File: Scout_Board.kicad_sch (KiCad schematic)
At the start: 6 parts, among them U1 DRV8871DDA, U2 ESP32-S3-DEVKITC-1U-N8R2

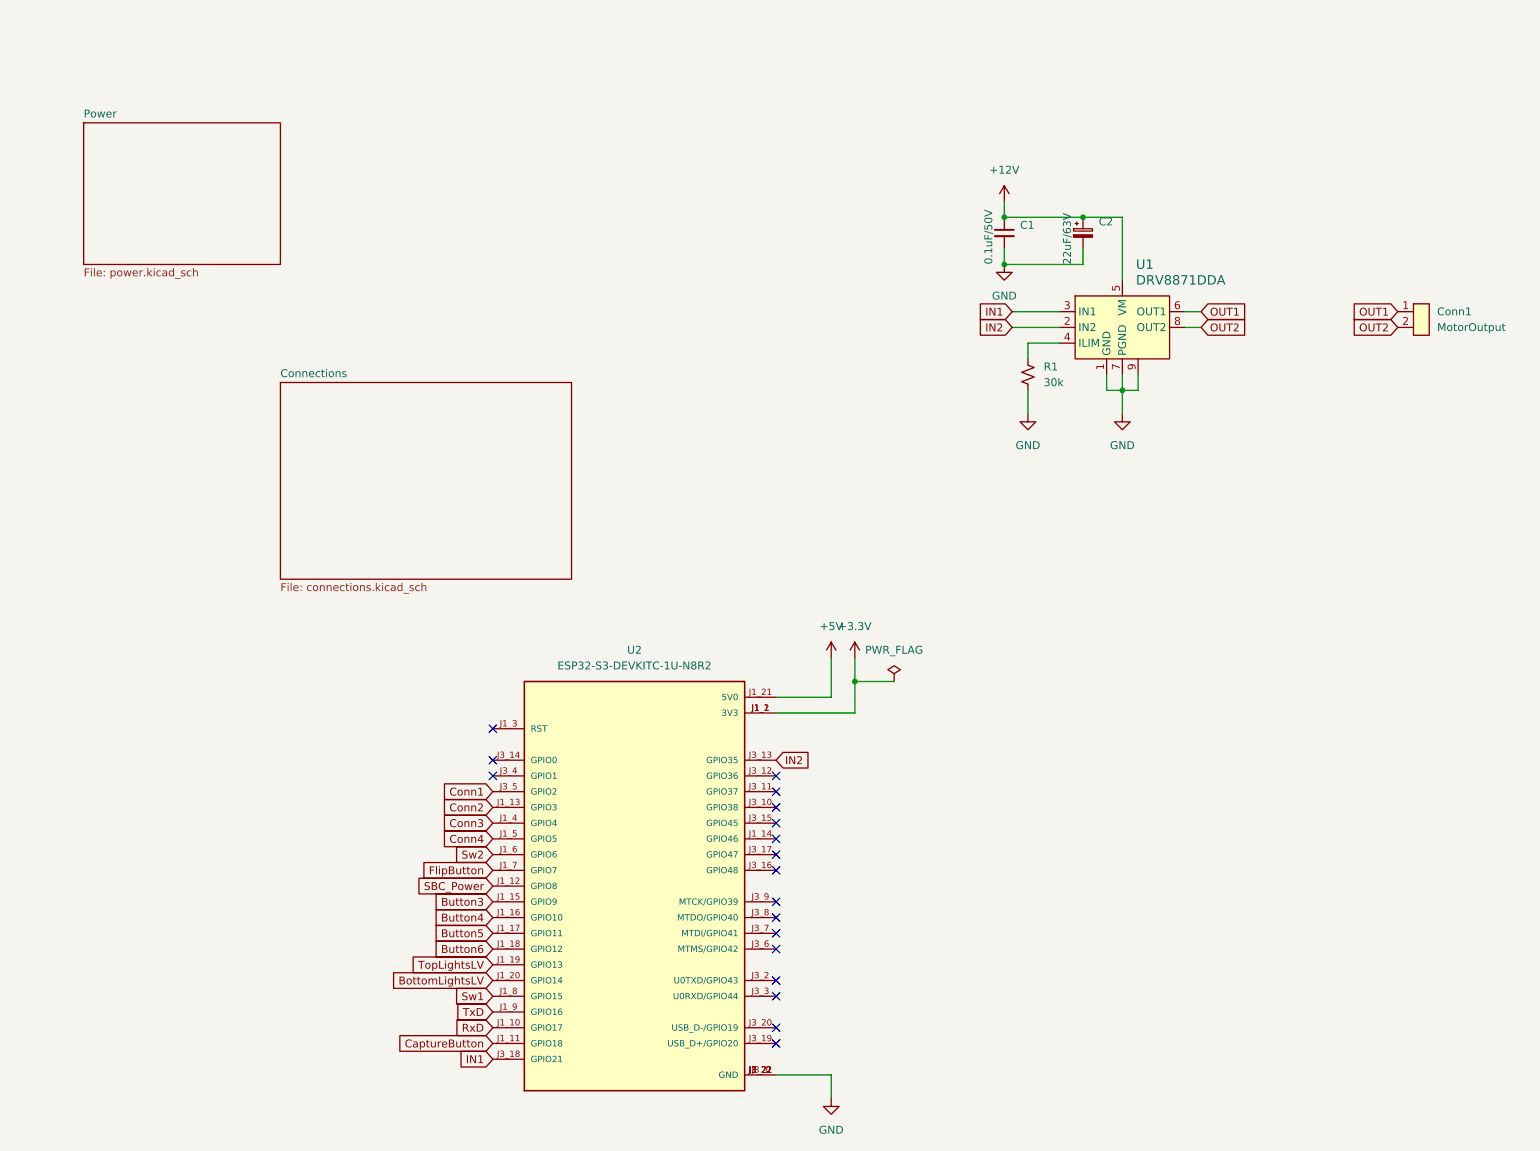
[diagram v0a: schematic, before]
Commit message: Removed motor and added A4988
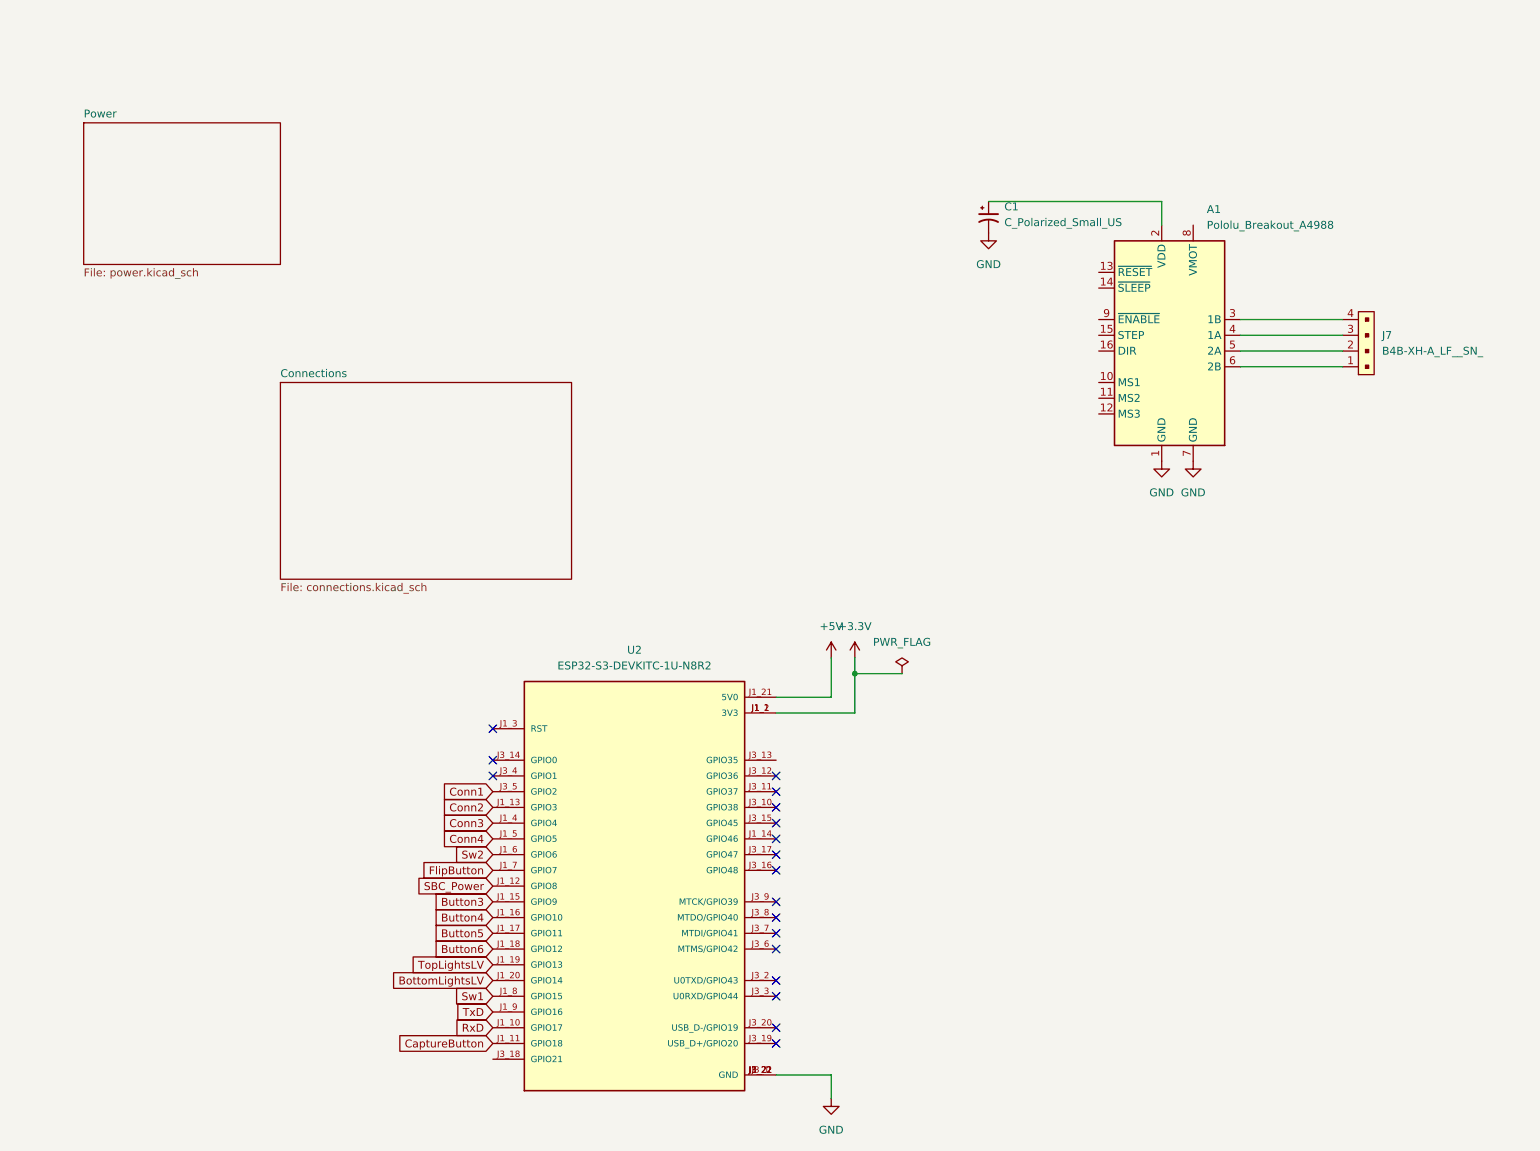
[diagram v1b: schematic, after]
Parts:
- removed C1: 0.1uF/50V, Capacitor_SMD:C_0603_1608Metric_Pad1.08x0.95mm_HandSolder, symbol Device:C_Small
- removed C2: 22uF/63V, EEH_ZA1J220XP:CAP_EEHZA1J220XP, symbol Device:C_Polarized_Small
- removed Conn1: MotorOutput, Downloaded_footprints:CONN_B2B-ZRLFSN_JST, symbol Scout_library:B2B_VERT_1.5MM
- removed R1: 30k, Resistor_SMD:R_0603_1608Metric_Pad0.98x0.95mm_HandSolder, symbol Device:R_Small_US
- removed U1: DRV8871DDA, Package_SO:Texas_HTSOP-8-1EP_3.9x4.9mm_P1.27mm_EP2.95x4.9mm_Mask2.4x3.1mm_ThermalVias, symbol dk_PMIC-Motor-Drivers-Controllers:DRV8871DDA
- added A1: Pololu_Breakout_A4988, Module:Pololu_Breakout-16_15.2x20.3mm, symbol Driver_Motor:Pololu_Breakout_A4988
- added C1: C_Polarized_Small_US, symbol Device:C_Polarized_Small_US
- added J7: B4B-XH-A_LF__SN_, digikey-footprints:PinHeader_1x4_P2mm_Drill1mm, symbol dk_Rectangular-Connectors-Headers-Male-Pins:B4B-XH-A_LF__SN_
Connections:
- net GND: now also A1.1 (GND), A1.7 (GND), C1.2
- net IN1: no longer names the net of U2.J3_18 (GPIO21)
- net IN2: no longer names the net of U2.J3_13 (GPIO35)
- new net: A1.2 (VDD), C1.1
- new net: A1.6 (2B), J7.1
- new net: A1.5 (2A), J7.2
- new net: A1.4 (1A), J7.3
- new net: A1.3 (1B), J7.4

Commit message: Added motor driver
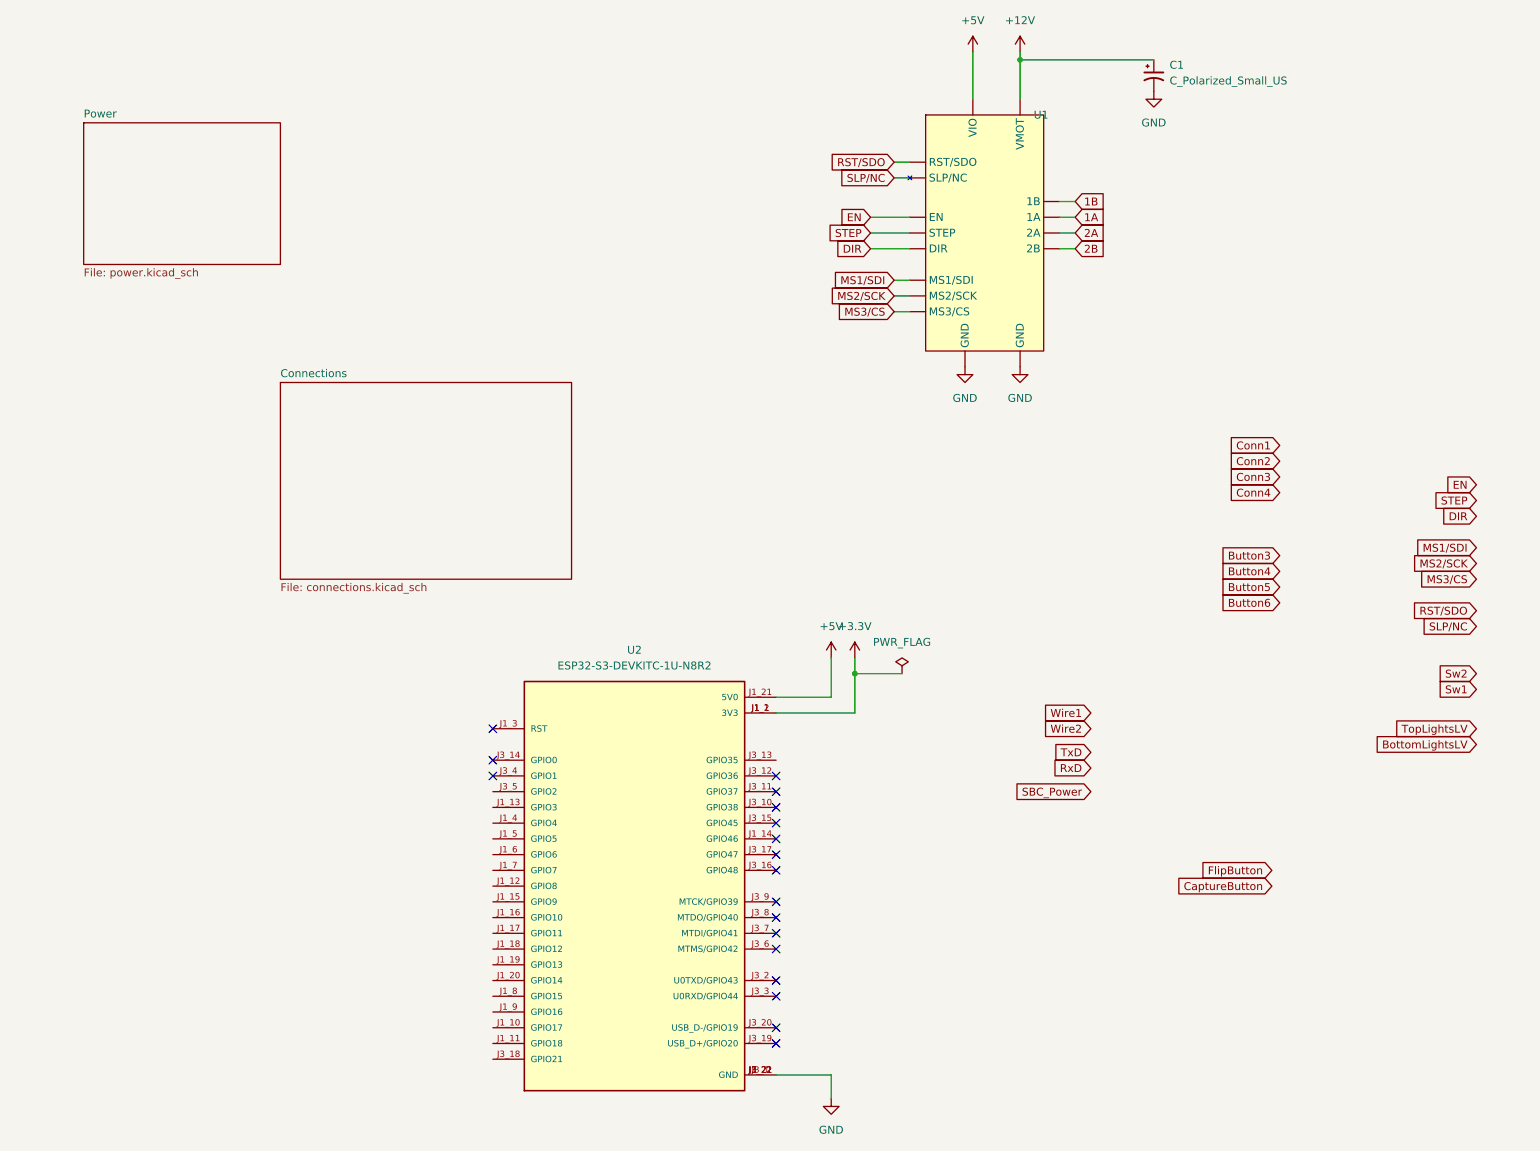
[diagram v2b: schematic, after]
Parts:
- removed A1: Pololu_Breakout_A4988, Module:Pololu_Breakout-16_15.2x20.3mm, symbol Driver_Motor:Pololu_Breakout_A4988
- removed J7: B4B-XH-A_LF__SN_, digikey-footprints:PinHeader_1x4_P2mm_Drill1mm, symbol dk_Rectangular-Connectors-Headers-Male-Pins:B4B-XH-A_LF__SN_
- added U1: ~, Module:Pololu_Breakout-16_15.2x20.3mm, symbol Custom Library:TMC2130
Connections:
- net +5V: now also U1. (SLP/NC)
- net BottomLightsLV: no longer U2.J1_20 (GPIO14)
- net Button3: no longer U2.J1_15 (GPIO9)
- net Button4: no longer U2.J1_16 (GPIO10)
- net Button5: no longer U2.J1_17 (GPIO11)
- net Button6: no longer U2.J1_18 (GPIO12)
- net CaptureButton: no longer U2.J1_11 (GPIO18)
- net Conn1: no longer U2.J3_5 (GPIO2)
- net Conn2: no longer U2.J1_13 (GPIO3)
- net Conn3: no longer U2.J1_4 (GPIO4)
- net Conn4: no longer U2.J1_5 (GPIO5)
- net FlipButton: no longer U2.J1_7 (GPIO7)
- net GND: now also U1. (SLP/NC)
- net RxD: no longer U2.J1_10 (GPIO17)
- net SBC_Power: no longer U2.J1_12 (GPIO8)
- net Sw1: no longer U2.J1_8 (GPIO15)
- net Sw2: no longer U2.J1_6 (GPIO6)
- net TopLightsLV: no longer U2.J1_19 (GPIO13)
- net TxD: no longer U2.J1_9 (GPIO16)
- net +12V: now reaches C1.1
- net +12V: now also U1. (SLP/NC)
- new net 1A: U1. (SLP/NC)
- new net 1B: U1. (SLP/NC)
- new net 2A: U1. (SLP/NC)
- new net 2B: U1. (SLP/NC)
- new net DIR: U1. (SLP/NC)
- new net EN: U1. (SLP/NC)
- new net MS1/SDI: U1. (SLP/NC)
- new net MS2/SCK: U1. (SLP/NC)
- new net MS3/CS: U1. (SLP/NC)
- new net RST/SDO: U1. (SLP/NC)
- new net SLP/NC: U1. (SLP/NC)
- new net STEP: U1. (SLP/NC)
